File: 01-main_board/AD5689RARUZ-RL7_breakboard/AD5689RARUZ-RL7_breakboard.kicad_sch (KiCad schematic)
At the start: 1 part, among them U1 AD5694ARUZ-RL7

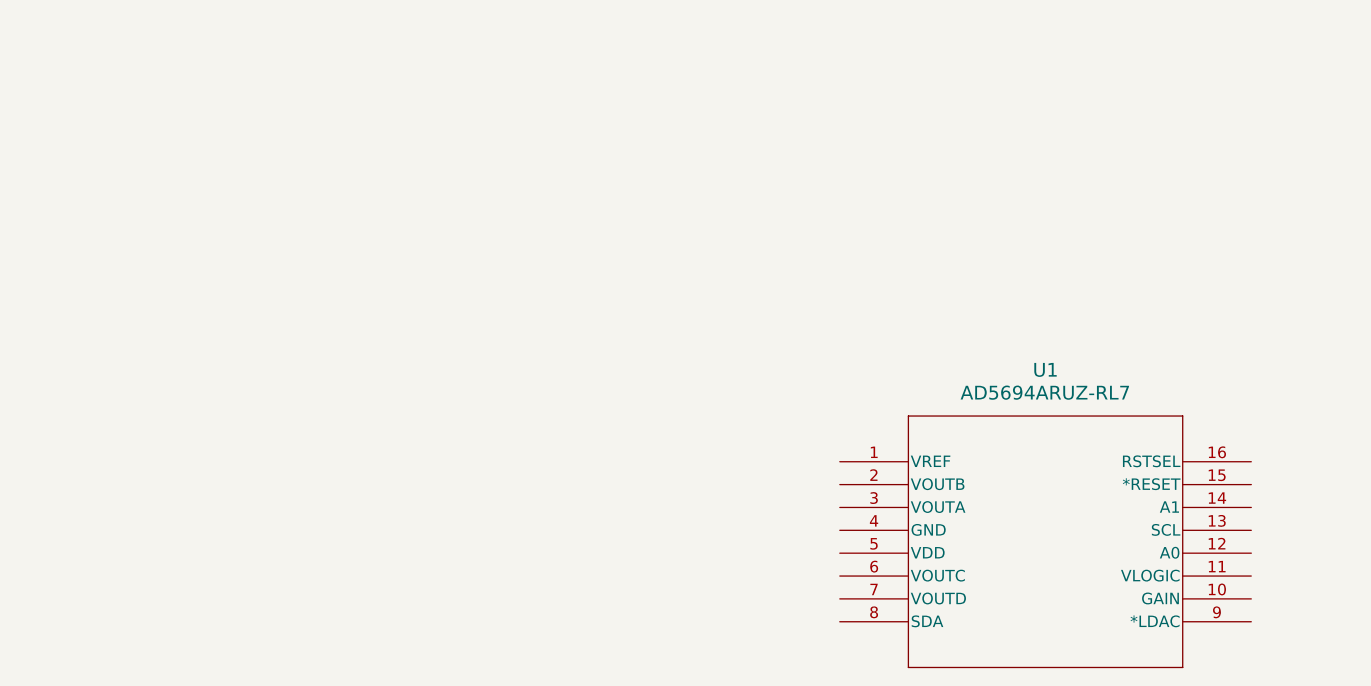
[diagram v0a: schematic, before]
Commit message: updated breakout
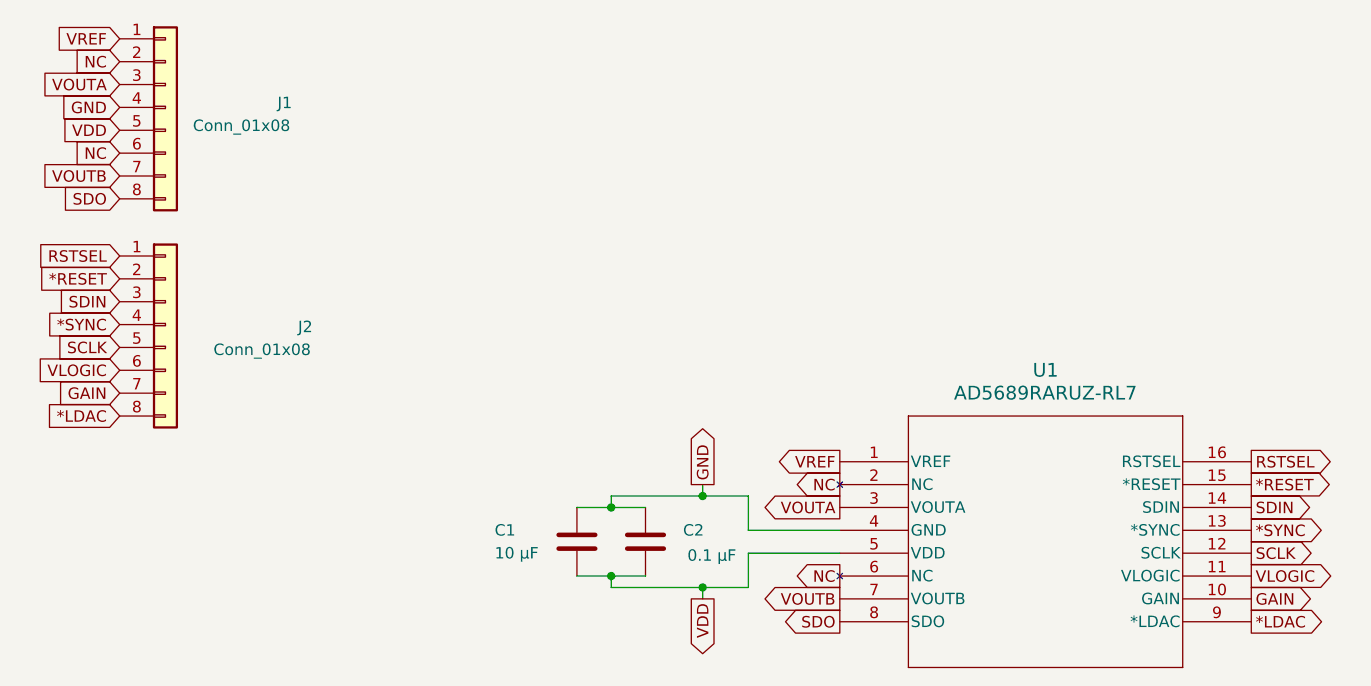
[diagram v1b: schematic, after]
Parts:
- removed U1: AD5694ARUZ-RL7, RU_16_ADI, symbol 2025-07-01_06-58-42:AD5694ARUZ-RL7
- added C1: 10 μF, Capacitor_SMD:C_0603_1608Metric, symbol Device:C
- added C2: 0.1 μF, Capacitor_SMD:C_0201_0603Metric, symbol Device:C
- added J1, J2: Conn_01x08, Connector_PinHeader_2.54mm:PinHeader_1x08_P2.54mm_Vertical, symbol Connector_Generic:Conn_01x08
- added U1: AD5689RARUZ-RL7, RU_16_ADI, symbol AD5689RARUZ-RL7_sym_lib:AD5689RARUZ-RL7
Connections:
- new net *LDAC: J2.8 (Pin_8), U1.9 (*LDAC)
- new net *RESET: J2.2 (Pin_2), U1.15 (*RESET)
- new net *SYNC: J2.4 (Pin_4), U1.13 (*SYNC)
- new net GAIN: J2.7 (Pin_7), U1.10 (GAIN)
- new net GND: C1.2, C2.2, J1.4 (Pin_4), U1.4 (GND)
- new net NC: J1.2 (Pin_2), J1.6 (Pin_6), U1.2 (NC), U1.6 (NC)
- new net RSTSEL: J2.1 (Pin_1), U1.16 (RSTSEL)
- new net SCLK: J2.5 (Pin_5), U1.12 (SCLK)
- new net SDIN: J2.3 (Pin_3), U1.14 (SDIN)
- new net SDO: J1.8 (Pin_8), U1.8 (SDO)
- new net VDD: C1.1, C2.1, J1.5 (Pin_5), U1.5 (VDD)
- new net VLOGIC: J2.6 (Pin_6), U1.11 (VLOGIC)
- new net VOUTA: J1.3 (Pin_3), U1.3 (VOUTA)
- new net VOUTB: J1.7 (Pin_7), U1.7 (VOUTB)
- new net VREF: J1.1 (Pin_1), U1.1 (VREF)

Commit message: updated breakout board
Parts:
- removed J1: Conn_01x08, Connector_PinHeader_2.54mm:PinHeader_1x08_P2.54mm_Vertical, symbol Connector_Generic:Conn_01x08
- added J1: Conn_01x06, Connector_PinHeader_2.54mm:PinHeader_1x06_P2.54mm_Vertical, symbol Connector_Generic:Conn_01x06
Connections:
- net GND: now also J1.3 (Pin_3)
- net SDO: now also J1.6 (Pin_6)
- net VDD: now also J1.4 (Pin_4)
- net VOUTA: now also J1.2 (Pin_2)
- net VOUTB: now also J1.5 (Pin_5)
- net VREF: now also J1.1 (Pin_1)
- net NC: no longer names the net of U1.2 (NC)
- net NC: no longer U1.6 (NC)
- no-connect marks 0 -> 2
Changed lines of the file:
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@@
 		(color 0 0 0 0)
 	)
+	(no_connect
+		(at 107.95 69.85)
+	)
+	(no_connect
+		(at 107.95 80.01)
+	)
 	(wire
 		(pts
@@
 	(global_label "VOUTB"
 		(shape input)
-		(at 27.94 35.56 180)
-		(fields_autoplaced yes)
-		(effects
-			(font
-				(size 1.27 1.27)
-			)
-			(justify right)
-		)
-		(property "Intersheetrefs" "${INTERSHEET_REFS}"
-			(at 18.9676 35.56 0)
+		(at 27.94 31.75 180)
+		(fields_autoplaced yes)
+		(effects
+			(font
+				(size 1.27 1.27)
+			)
+			(justify right)
+		)
+		(property "Intersheetrefs" "${INTERSHEET_REFS}"
+			(at 18.9676 31.75 0)
 			(effects
 				(font
@@
 		)
 	)
-	(global_label "NC"
-		(shape output)
-		(at 107.95 80.01 180)
-		(fields_autoplaced yes)
-		(effects
-			(font
-				(size 1.27 1.27)
-			)
-			(justify right)
-		)
-		(property "Intersheetrefs" "${INTERSHEET_REFS}"
-			(at 102.3643 80.01 0)
-			(effects
-				(font
-					(size 1.27 1.27)
-				)
-				(justify right)
-				(hide yes)
-			)
-		)
-	)
-	(global_label "NC"
-		(shape input)
-		(at 27.94 33.02 180)
-		(fields_autoplaced yes)
-		(effects
-			(font
-				(size 1.27 1.27)
-			)
-			(justify right)
-		)
-		(property "Intersheetrefs" "${INTERSHEET_REFS}"
-			(at 22.3543 33.02 0)
-			(effects
-				(font
-					(size 1.27 1.27)
-				)
-				(justify right)
-				(hide yes)
-			)
-		)
-	)
-	(global_label "NC"
-		(shape input)
-		(at 27.94 22.86 180)
-		(fields_autoplaced yes)
-		(effects
-			(font
-				(size 1.27 1.27)
-			)
-			(justify right)
-		)
-		(property "Intersheetrefs" "${INTERSHEET_REFS}"
-			(at 22.3543 22.86 0)
-			(effects
-				(font
-					(size 1.27 1.27)
-				)
-				(justify right)
-				(hide yes)
-			)
-		)
-	)
 	(global_label "VREF"
 		(shape output)
@@
 		)
 	)
-	(global_label "NC"
-		(shape output)
-		(at 107.95 69.85 180)
-		(fields_autoplaced yes)
-		(effects
-			(font
-				(size 1.27 1.27)
-			)
-			(justify right)
-		)
-		(property "Intersheetrefs" "${INTERSHEET_REFS}"
-			(at 102.3643 69.85 0)
-			(effects
-				(font
-					(size 1.27 1.27)
-				)
-				(justify right)
-				(hide yes)
-			)
-		)
-	)
 	(global_label "*SYNC"
 		(shape input)
@@
 	(global_label "VOUTA"
 		(shape input)
-		(at 27.94 25.4 180)
-		(fields_autoplaced yes)
-		(effects
-			(font
-				(size 1.27 1.27)
-			)
-			(justify right)
-		)
-		(property "Intersheetrefs" "${INTERSHEET_REFS}"
-			(at 19.149 25.4 0)
+		(at 27.94 24.13 180)
+		(fields_autoplaced yes)
+		(effects
+			(font
+				(size 1.27 1.27)
+			)
+			(justify right)
+		)
+		(property "Intersheetrefs" "${INTERSHEET_REFS}"
+			(at 19.149 24.13 0)
 			(effects
 				(font
@@
 	(global_label "VDD"
 		(shape input)
-		(at 27.94 30.48 180)
-		(fields_autoplaced yes)
-		(effects
-			(font
-				(size 1.27 1.27)
-			)
-			(justify right)
-		)
-		(property "Intersheetrefs" "${INTERSHEET_REFS}"
-			(at 21.3262 30.48 0)
+		(at 27.94 29.21 180)
+		(fields_autoplaced yes)
+		(effects
+			(font
+				(size 1.27 1.27)
+			)
+			(justify right)
+		)
+		(property "Intersheetrefs" "${INTERSHEET_REFS}"
+			(at 21.3262 29.21 0)
 			(effects
 				(font
@@
 	(global_label "SDO"
 		(shape input)
-		(at 27.94 38.1 180)
-		(fields_autoplaced yes)
-		(effects
-			(font
-				(size 1.27 1.27)
-			)
-			(justify right)
-		)
-		(property "Intersheetrefs" "${INTERSHEET_REFS}"
-			(at 21.1448 38.1 0)
+		(at 27.94 34.29 180)
+		(fields_autoplaced yes)
+		(effects
+			(font
+				(size 1.27 1.27)
+			)
+			(justify right)
+		)
+		(property "Intersheetrefs" "${INTERSHEET_REFS}"
+			(at 21.1448 34.29 0)
 			(effects
 				(font
@@
 	(global_label "GND"
 		(shape input)
-		(at 27.94 27.94 180)
-		(fields_autoplaced yes)
-		(effects
-			(font
-				(size 1.27 1.27)
-			)
-			(justify right)
-		)
-		(property "Intersheetrefs" "${INTERSHEET_REFS}"
-			(at 21.0843 27.94 0)
+		(at 27.94 26.67 180)
+		(fields_autoplaced yes)
+		(effects
+			(font
+				(size 1.27 1.27)
+			)
+			(justify right)
+		)
+		(property "Intersheetrefs" "${INTERSHEET_REFS}"
+			(at 21.0843 26.67 0)
 			(effects
 				(font
@@
 	(global_label "VREF"
 		(shape input)
-		(at 27.94 20.32 180)
-		(fields_autoplaced yes)
-		(effects
-			(font
-				(size 1.27 1.27)
-			)
-			(justify right)
-		)
-		(property "Intersheetrefs" "${INTERSHEET_REFS}"
-			(at 20.3586 20.32 0)
+		(at 27.94 21.59 180)
+		(fields_autoplaced yes)
+		(effects
+			(font
+				(size 1.27 1.27)
+			)
+			(justify right)
+		)
+		(property "Intersheetrefs" "${INTERSHEET_REFS}"
+			(at 20.3586 21.59 0)
 			(effects
 				(font
@@
 				(path "/089f745c-fcf3-4ebd-ba21-42df85986f29"
 					(reference "U1")
+					(unit 1)
+				)
+			)
+		)
+	)
+	(symbol
+		(lib_id "Connector_Generic:Conn_01x06")
+		(at 33.02 26.67 0)
+		(unit 1)
+		(exclude_from_sim no)
+		(in_bom yes)
+		(on_board yes)
+		(dnp no)
+		(fields_autoplaced yes)
+		(property "Reference" "J1"
+			(at 35.56 26.6699 0)
+			(effects
+				(font
+					(size 1.27 1.27)
+				)
+				(justify left)
+			)
+		)
+		(property "Value" "Conn_01x06"
+			(at 35.56 29.2099 0)
+			(effects
+				(font
+					(size 1.27 1.27)
+				)
+				(justify left)
+			)
+		)
+		(property "Footprint" "Connector_PinHeader_2.54mm:PinHeader_1x06_P2.54mm_Vertical"
+			(at 33.02 26.67 0)
+			(effects
+				(font
+					(size 1.27 1.27)
+				)
+				(hide yes)
+			)
+		)
+		(property "Datasheet" "~"
+			(at 33.02 26.67 0)
+			(effects
+				(font
+					(size 1.27 1.27)
+				)
+				(hide yes)
+			)
+		)
+		(property "Description" "Generic connector, single row, 01x06, script generated (kicad-library-utils/schlib/autogen/connector/)"
+			(at 33.02 26.67 0)
+			(effects
+				(font
+					(size 1.27 1.27)
+				)
+				(hide yes)
+			)
+		)
+		(pin "1"
+		)
+		(pin "2"
+		)
+		(pin "3"
+		)
+		(pin "4"
+		)
+		(pin "5"
+		)
+		(pin "6"
+		)
+		(instances
+			(project ""
+				(path "/089f745c-fcf3-4ebd-ba21-42df85986f29"
+					(reference "J1")
 					(unit 1)
 				)
@@
 					(unit 1)
 				)
-			)
-		)
-	)
-	(symbol
-		(lib_id "Connector_Generic:Conn_01x08")
-		(at 33.02 27.94 0)
-		(unit 1)
-		(exclude_from_sim no)
-		(in_bom yes)
-		(on_board yes)
-		(dnp no)
-		(property "Reference" "J1"
-			(at 45.466 27.432 0)
-			(effects
-				(font
-					(size 1.27 1.27)
-				)
-				(justify left)
-			)
-		)
-		(property "Value" "Conn_01x08"
-			(at 36.068 29.972 0)
-			(effects
-				(font
-					(size 1.27 1.27)
-				)
-				(justify left)
-			)
-		)
-		(property "Footprint" "Connector_PinHeader_2.54mm:PinHeader_1x08_P2.54mm_Vertical"
-			(at 33.02 27.94 0)
-			(effects
-				(font
-					(size 1.27 1.27)
-				)
-				(hide yes)
-			)
-		)
-		(property "Datasheet" "~"
-			(at 33.02 27.94 0)
-			(effects
-				(font
-					(size 1.27 1.27)
-				)
-				(hide yes)
-			)
-		)
-		(property "Description" "Generic connector, single row, 01x08, script generated (kicad-library-utils/schlib/autogen/connector/)"
-			(at 33.02 27.94 0)
-			(effects
-				(font
-					(size 1.27 1.27)
-				)
-				(hide yes)
-			)
-		)
-		(pin "1"
-		)
-		(pin "5"
-		)
-		(pin "6"
-		)
-		(pin "4"
-		)
-		(pin "3"
-		)
-		(pin "2"
-		)
-		(pin "7"
-		)
-		(pin "8"
-		)
-		(instances
-			(project ""
-				(path "/089f745c-fcf3-4ebd-ba21-42df85986f29"
-					(reference "J1")
-					(unit 1)
-				)
